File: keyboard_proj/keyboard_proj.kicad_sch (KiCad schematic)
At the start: 13 parts

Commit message: Tous les schematics vérifiés 1x
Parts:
- removed IC?: USBLC6-4SC6, SOT95P280X145-6N, symbol SamacSys_Parts:USBLC6-2SC6
- added D?: LED, symbol Device:LED
- added R?: 1k, symbol Device:R
- added R?: 100, symbol Device:R
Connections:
- net GND: now also C?.2, R?.1, R?.1; no longer C?.1
- net OSC32_OUT: now also C?.1; no longer C?.2
- net at U?.4 (PH3-BOOT0): now also R?.2
- net stby: now reaches U?.46 (PB6)
- net chrg: now reaches U?.47 (PB7)
- net OSC_IN: no longer names the net of U?.1
- net OSC_IN: now also U?.24 (OSC_OUT); no longer U?.25 (OSC_IN)
- net OSC_OUT: no longer names the net of U?.2
- net OSC_OUT: now also U?.25 (OSC_IN); no longer U?.24 (OSC_OUT)
- net PB5: no longer names the net of U?.45 (PB5)
- net PB5: now also D?.2 (A)
- new net: D?.1 (K), R?.2
- no-connect marks 0 -> 2
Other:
- sheet Power ports: added 3.3V, D+, D-; removed 1.8V
- sheet battery_mgmnt ports: added none; removed Vbat+, Vbat-
- note added: "Reserved"
- moved on the sheet: C?, U?

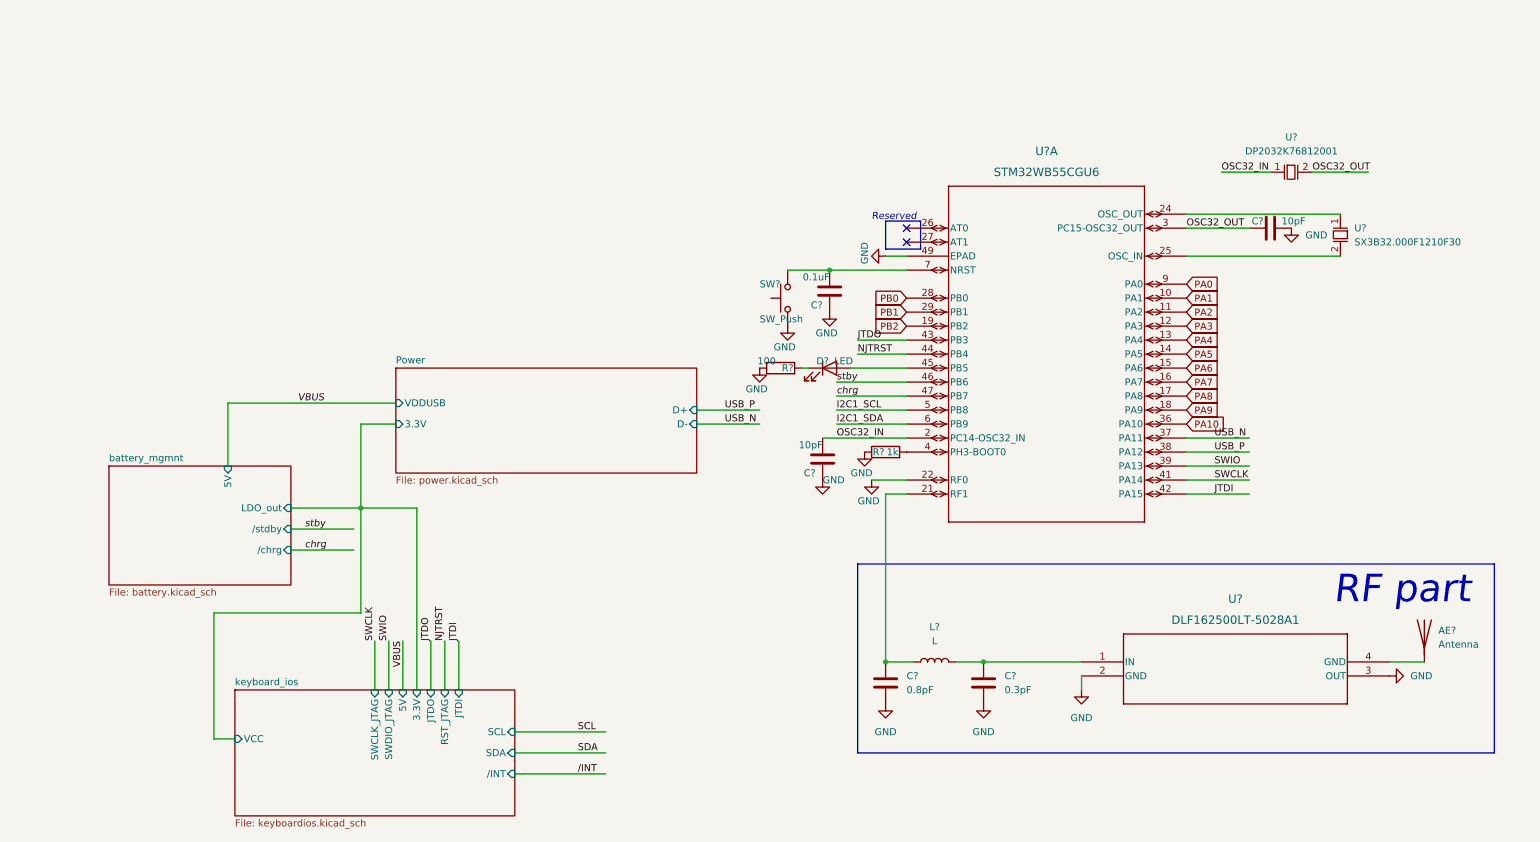
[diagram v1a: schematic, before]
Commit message: Ajout backlight et light sensor (in progress)
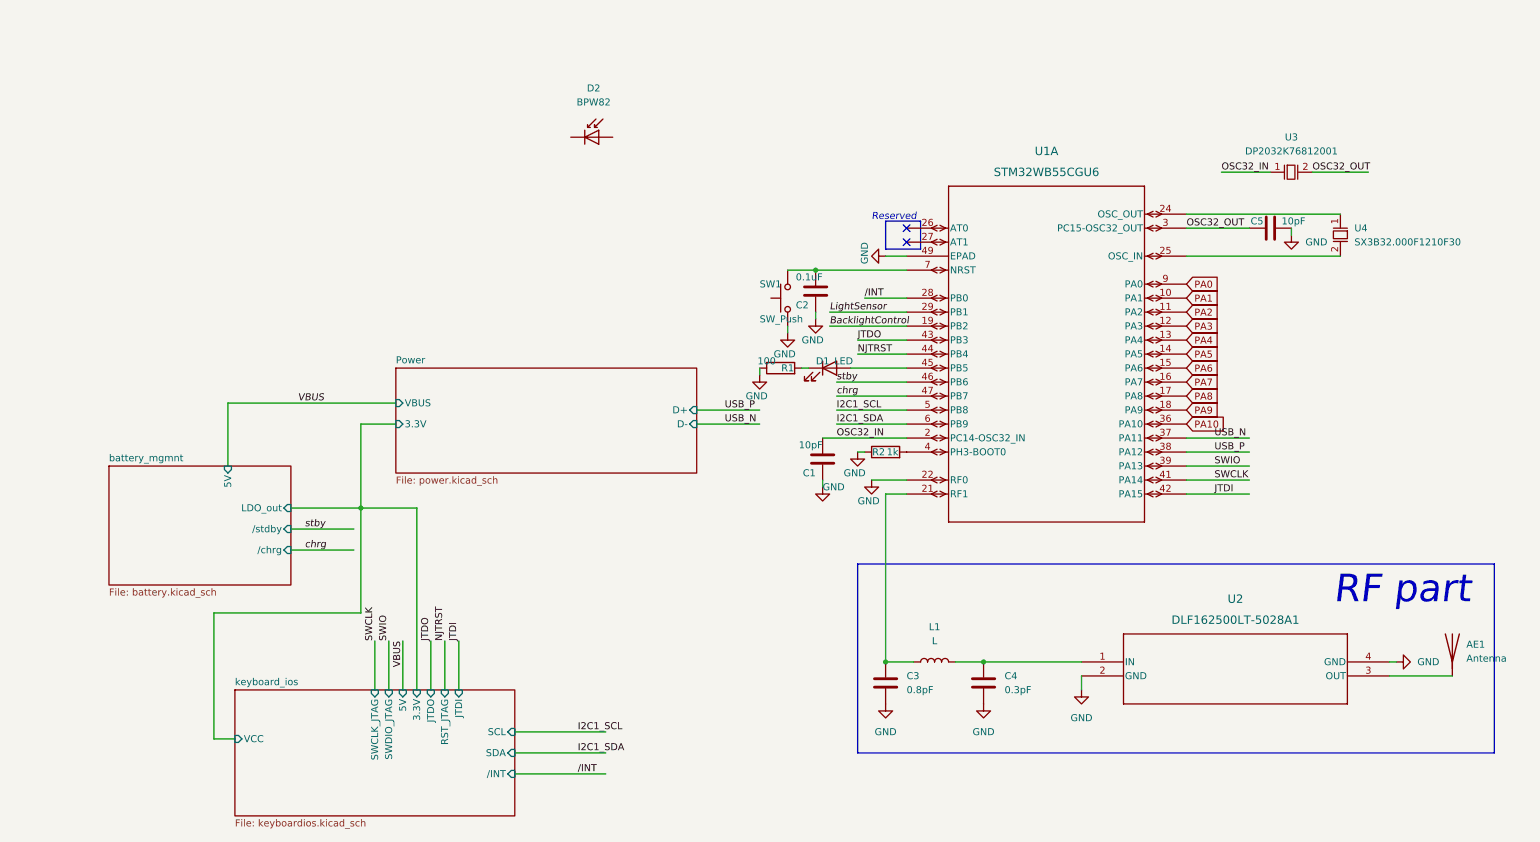
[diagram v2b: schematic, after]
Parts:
- added D2: BPW82, OptoDevice:Osram_BPW82, symbol Sensor_Optical:BPW82
- gave numbers to parts that had none: 15
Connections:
- net PB0 is gone; now on net /INT: U1.28 (PB0)
- net GND: now also U2.4 (GND); no longer U2.3 (OUT)
- net at AE1.1 (A): now also U2.3 (OUT); no longer U2.4 (GND)
- net PB1 renamed LightSensor
- net PB2 renamed BacklightControl
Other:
- sheet Power ports: added VBUS; removed VDDUSB
- moved on the sheet: AE1, C2

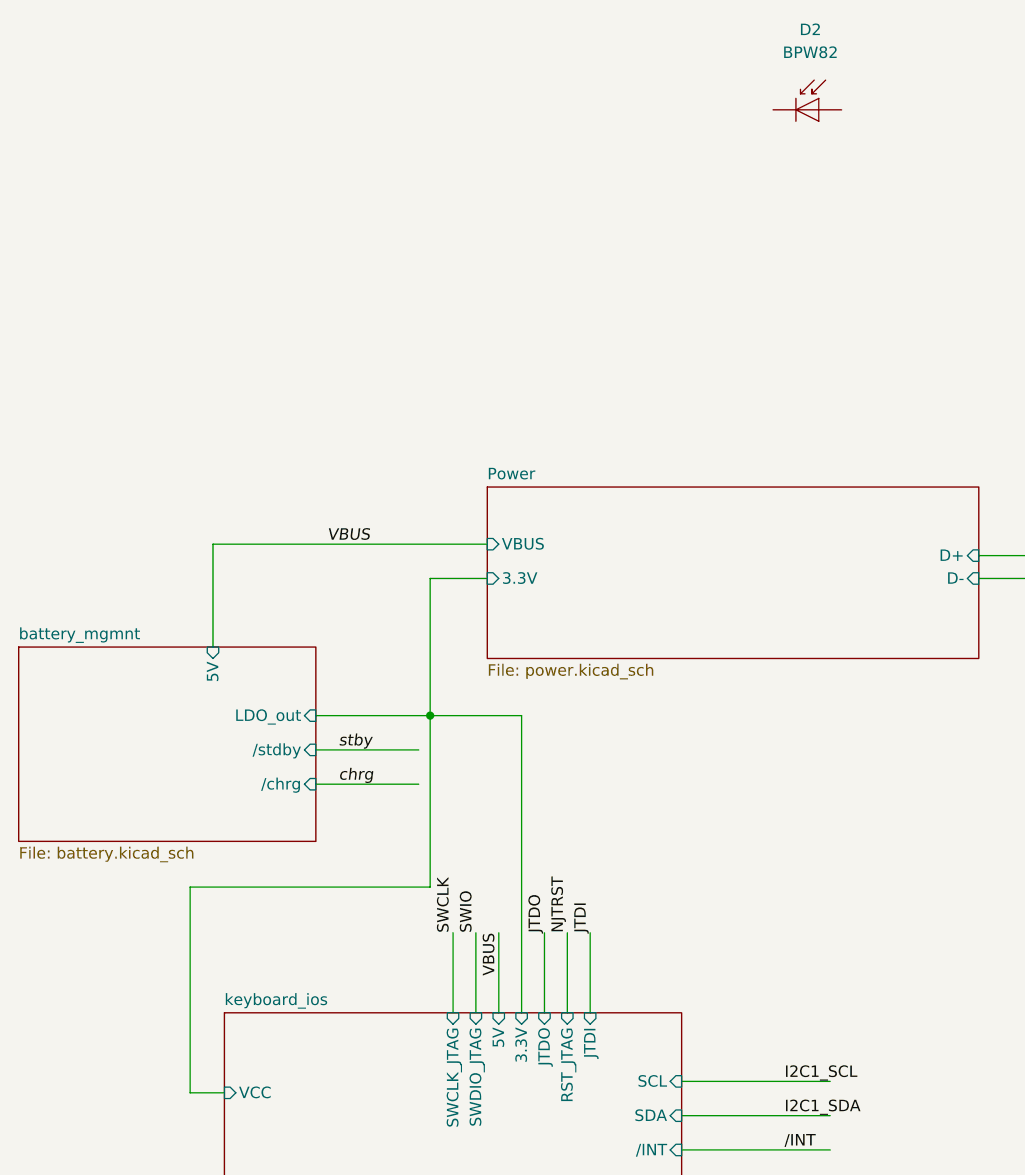
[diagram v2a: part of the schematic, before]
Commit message: Ajout light sensor et controle avec mosfet pour backlight
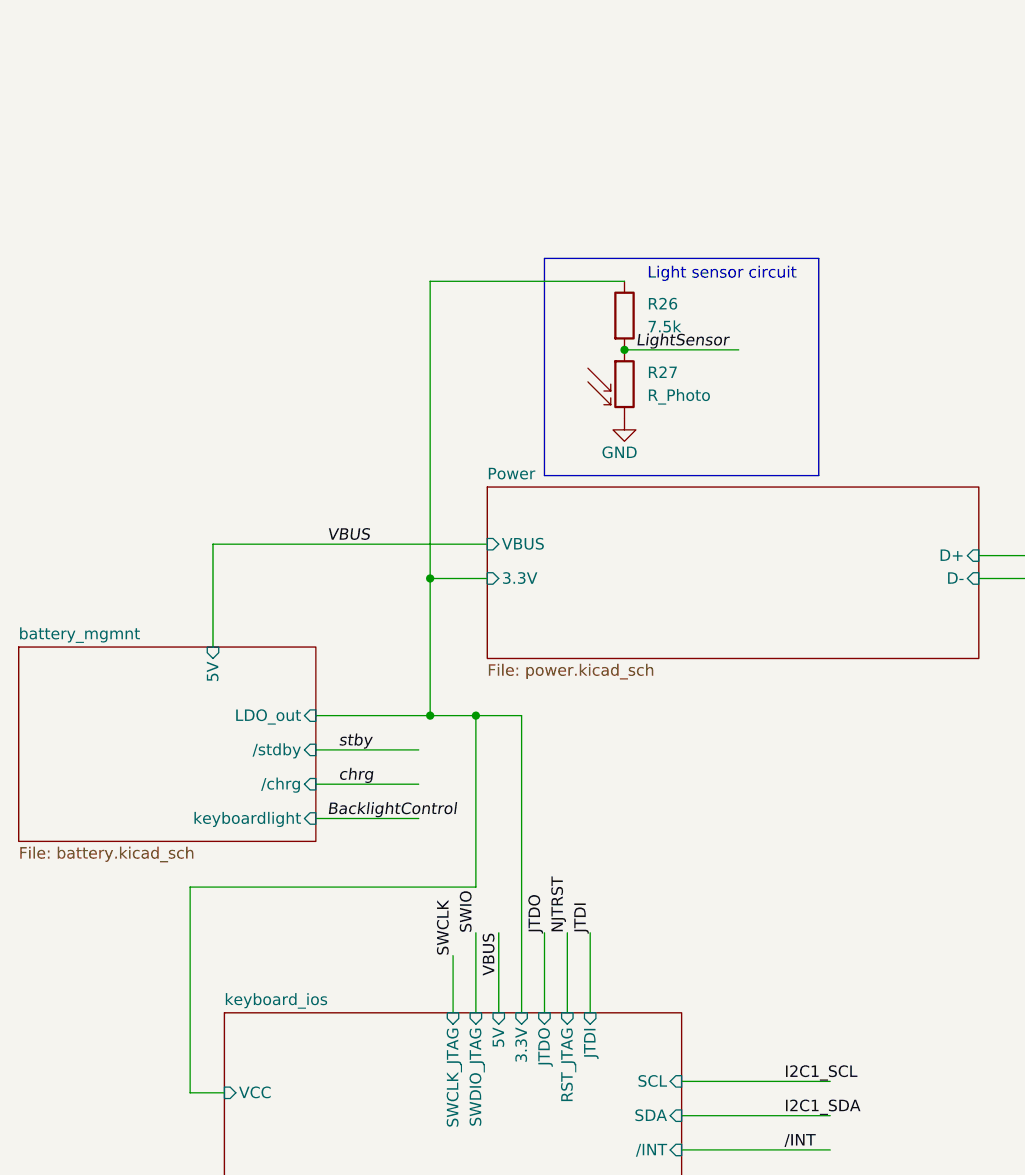
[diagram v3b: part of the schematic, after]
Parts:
- removed D2: BPW82, OptoDevice:Osram_BPW82, symbol Sensor_Optical:BPW82
- added R26: 7.5k, symbol Device:R
- added R27: R_Photo, symbol Device:R_Photo
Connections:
- net GND: now also R27.2
- net LightSensor: now also R26.2, R27.1
- net Power/3.3V: now also R26.1
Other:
- sheet battery_mgmnt ports: added keyboardlight; removed none
- note added: "Light sensor circuit"

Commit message: Ajout des empreintes, il en manque encore
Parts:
- AE1: footprint (none) -> SamacSys_Parts:BLE_PCB_ant
- C1, C2, C3, C4, C5: footprint (none) -> Capacitor_SMD:C_0402_1005Metric
- D1: footprint (none) -> LED_SMD:LED_0603_1608Metric
- L1: value L -> 2.7nH; footprint (none) -> Inductor_SMD:L_0402_1005Metric
- R1, R2, R26: footprint (none) -> Resistor_SMD:R_0402_1005Metric
- U1: footprint UFQFPN48-7x7mm -> STM32WB:UFQFPN48-7x7mm
- U2: footprint DLF-4_1P6X0P8 -> DLF162500LT-5028A1:DLF-4_1P6X0P8
- U3: footprint (none) -> SamacSys_Parts:Quartz-HC-49S-SMD-Mini
- U4: footprint (none) -> SamacSys_Parts:Quartz-SMD3225-4P

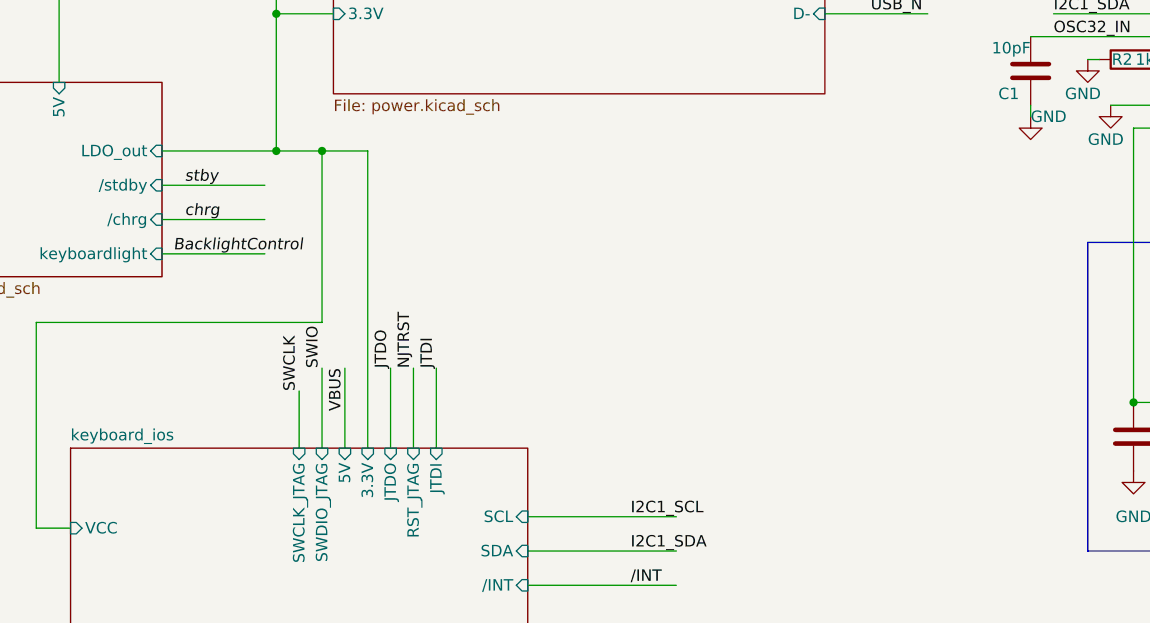
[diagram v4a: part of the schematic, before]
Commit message: Empreintes finies, besoin de reverifier, disposition des composants sur la carte
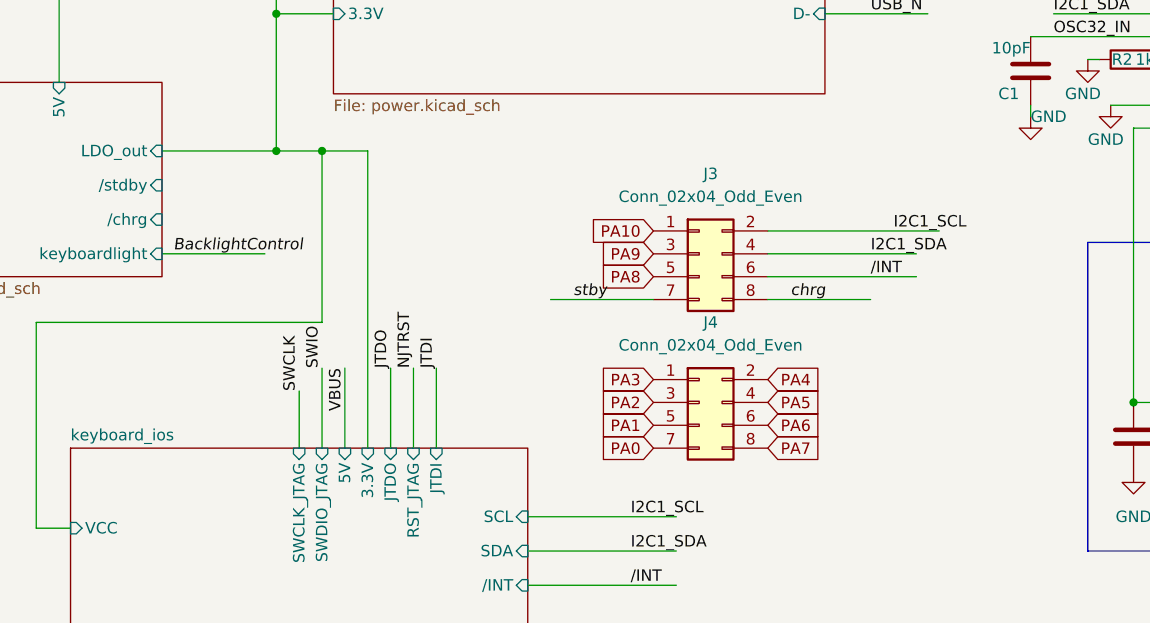
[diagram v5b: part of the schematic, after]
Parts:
- added J3, J4: Conn_02x04_Odd_Even, SamacSys_Parts:debug_conn, symbol Connector_Generic:Conn_02x04_Odd_Even
- R27: footprint (none) -> SamacSys_Parts:R_photo
- SW1: footprint (none) -> SamacSys_Parts:switch
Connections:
- net I2C1_SCL: now also J3.2 (Pin_2)
- net I2C1_SDA: now also J3.4 (Pin_4)
- net PA0: now also J4.7 (Pin_7)
- net PA1: now also J4.5 (Pin_5)
- net PA10: now also J3.1 (Pin_1)
- net PA2: now also J4.3 (Pin_3)
- net PA3: now also J4.1 (Pin_1)
- net PA4: now also J4.2 (Pin_2)
- net PA5: now also J4.4 (Pin_4)
- net PA6: now also J4.6 (Pin_6)
- net PA7: now also J4.8 (Pin_8)
- net PA8: now also J3.5 (Pin_5)
- net PA9: now also J3.3 (Pin_3)
- net chrg: now also J3.8 (Pin_8)
- net stby: now also J3.7 (Pin_7)
- net /INT: now also J3.6 (Pin_6)

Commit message: PCB bien avancé, presque fini mais je dois selectionner des pieces de jlcpcb pour baisser les couts
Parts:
- C1, C5: LCSC (none) -> C482482
- C2: value 0.1uF -> 100nF; LCSC (none) -> C880603
- C3: LCSC (none) -> C76988
- C4: LCSC (none) -> C92338
- D1: LCSC (none) -> C7429910
- J3, J4: LCSC (none) -> C376087
- L1: LCSC (none) -> C77108
- R1: value 100 -> 100Ω; LCSC (none) -> C304972
- R2: value 1k -> 1kΩ; LCSC (none) -> C2909306
- R26: LCSC (none) -> C100526
- R27: LCSC (none) -> C125626
- SW1: LCSC (none) -> C2909692
- U1: LCSC (none) -> C404023
- U2: LCSC (none) -> C531364
- U3: LCSC (none) -> C17702403
- U4: LCSC (none) -> C2901706
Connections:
- net GND: now also C2.2; no longer C2.1
- net at SW1.2, U1.7 (NRST): now also C2.1; no longer C2.2
